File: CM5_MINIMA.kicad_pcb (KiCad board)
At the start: 4 copper layers, 54.6 x 57.1 mm, 98 parts, among them J101 USB_C_Receptacle_USB2.0, J501 690-019-298-412, J502 I2C, J601 JST_SHBM04B-SRSS-TB, Q501 DTC043ZEBTL, SW501 SW_Push, SW601 B3U-3000P, SW602 B3U-3000P, T401 7498111120AR, U401 TPD4EUSB30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

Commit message: DRC ok
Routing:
- net Net-(T401-SHIELD1): track 31.3 -> 33.5 mm

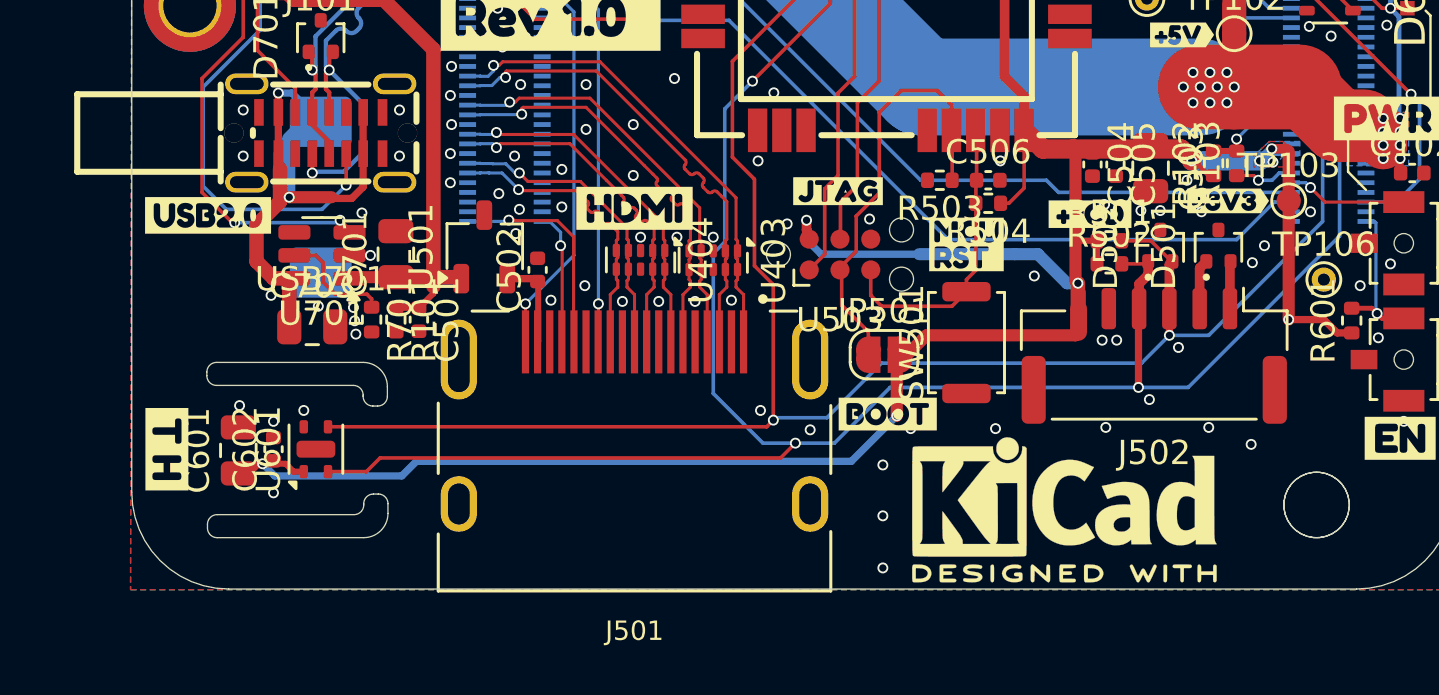
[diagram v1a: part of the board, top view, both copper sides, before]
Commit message: round slot TH
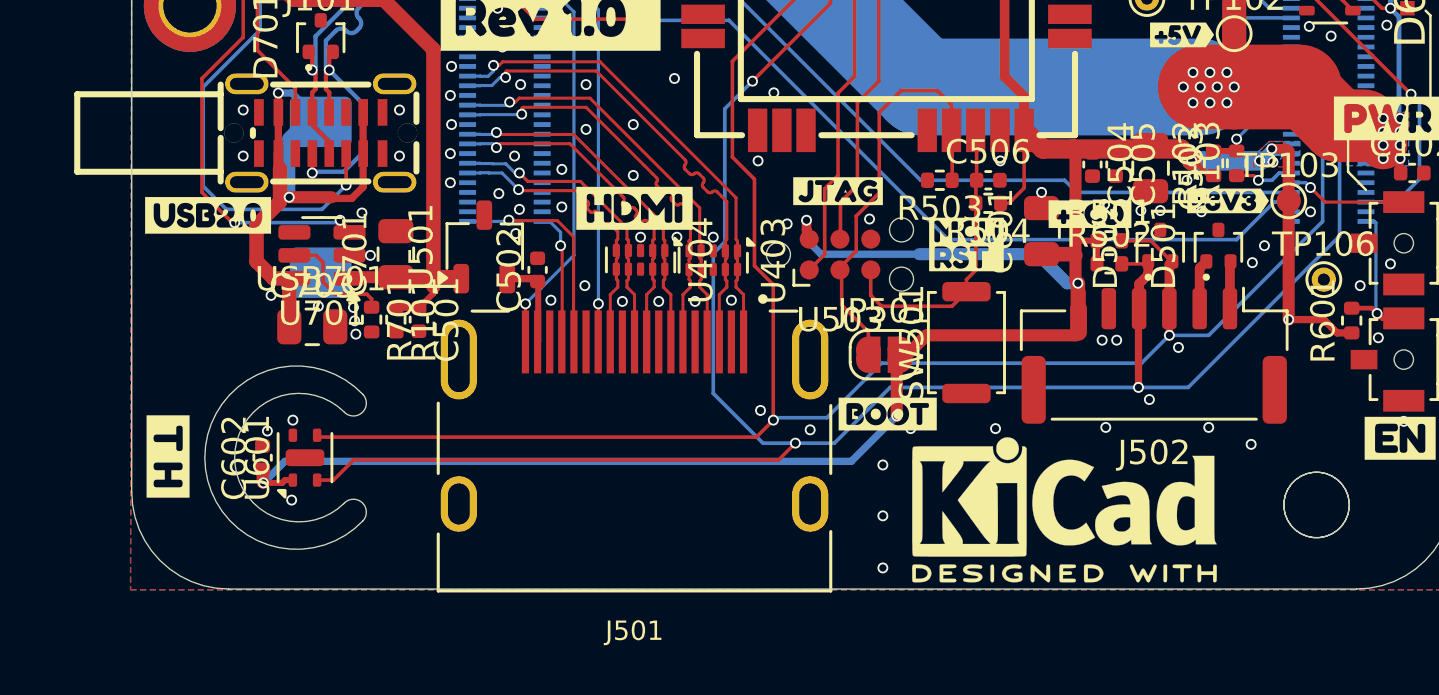
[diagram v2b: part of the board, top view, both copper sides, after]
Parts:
- moved C601 34.4 mm to (115.9, 66.3)
- moved C602 0.57 mm to (83.8, 75.7)
- moved U601 0.57 mm to (85.5, 75.7)
- moved kibuzzard-675DCF7A 0.30 mm to (79.8, 75.6)
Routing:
- net +3V3: track 153.1 -> 153.7 mm
- net /SDA: track 83.0 -> 83.7 mm
- net /SCL: track 90.0 -> 90.6 mm
- net GND: vias 199 -> 198
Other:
- outline, holes or cut-outs redrawn

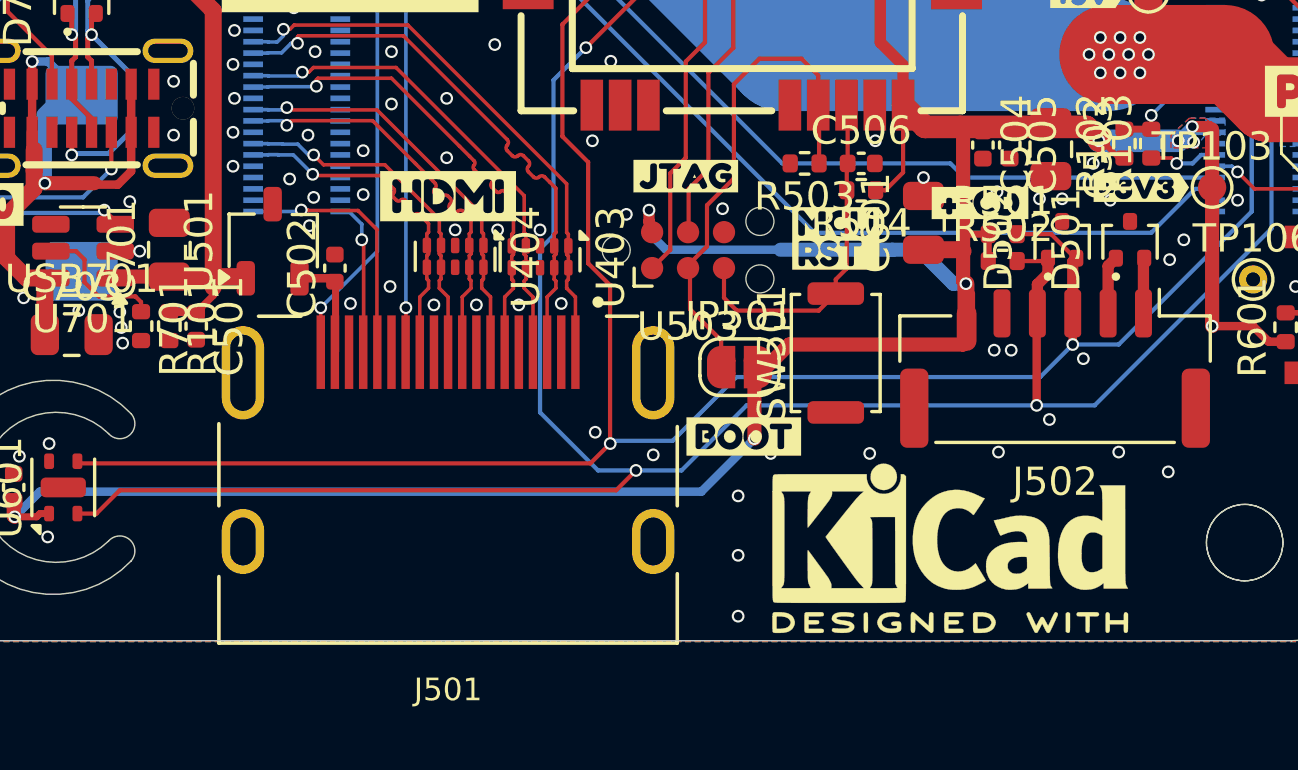
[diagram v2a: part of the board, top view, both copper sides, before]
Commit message: changed switch on HDMI
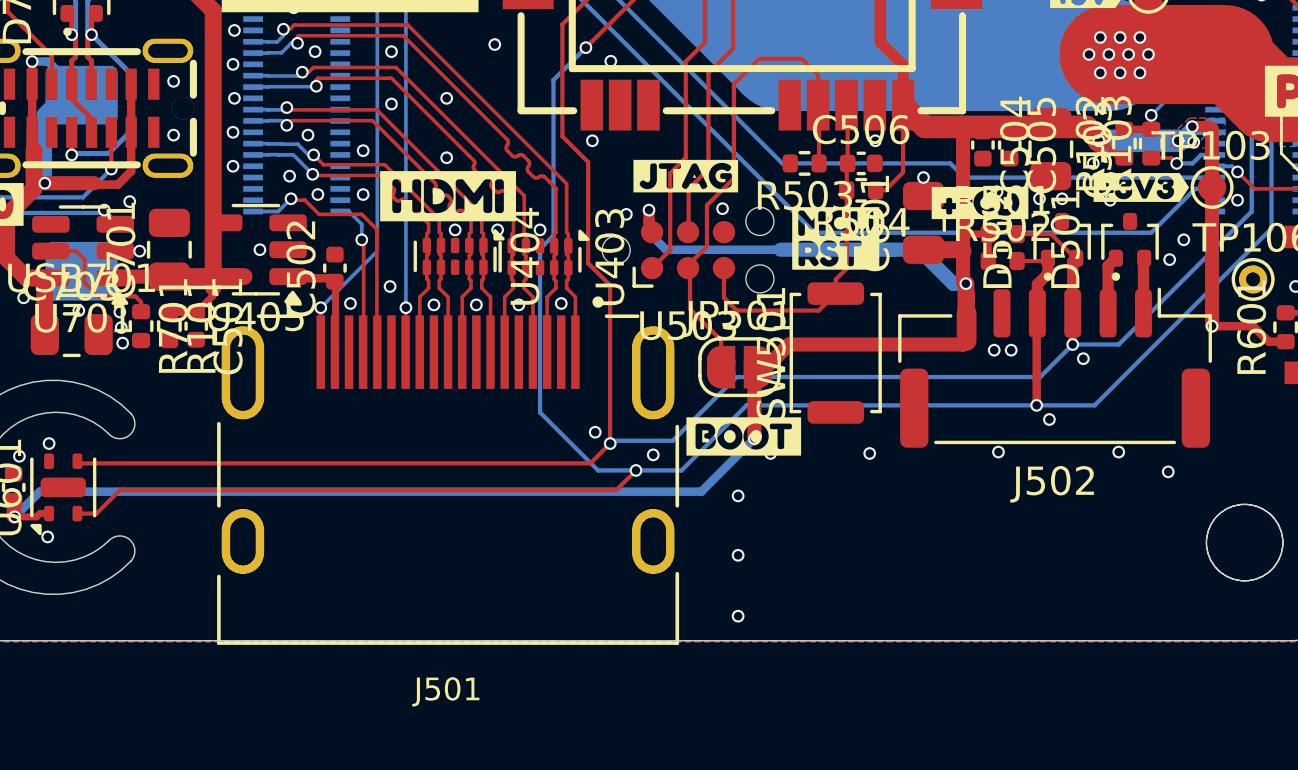
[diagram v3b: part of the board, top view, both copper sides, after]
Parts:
- removed the REF** at (116.8, 77.8)
- removed U501: RT9742SNGV, Package_TO_SOT_SMD:TSOT-23
- added U405: STMPS2151STR, Package_TO_SOT_SMD:SOT-23-5, F.Cu at (92.3, 67.2)
